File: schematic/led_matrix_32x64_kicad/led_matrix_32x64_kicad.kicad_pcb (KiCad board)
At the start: 2 copper layers, 6 parts, among them J1 LED Interface, J2 RTC, J3 INTERFACE, SW3 RESET, U1 Pico

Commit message: Snapshot before flipping the board
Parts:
- added C2: 1u, Capacitor_SMD:C_0805_2012Metric_Pad1.18x1.45mm_HandSolder, F.Cu at (114.7, 66.0)
- added C3: 1u, Capacitor_SMD:C_0805_2012Metric_Pad1.18x1.45mm_HandSolder, F.Cu at (116.0, 79.6)
- added J4: LEDPWR, Connector_PinHeader_2.54mm:PinHeader_1x02_P2.54mm_Horizontal, B.Cu at (115.3, 62.5)
- added R1: 10k, Resistor_SMD:R_0805_2012Metric_Pad1.20x1.40mm_HandSolder, F.Cu at (115.1, 75.6)
- added U2: NCP380, Package_SO:TSOP-5_1.65x3.05mm_P0.95mm, F.Cu at (114.7, 71.1)
- moved C1 47.5 mm to (116.6, 93.3), turned to 180 degrees
- moved SW3 28.4 mm to (110.9, 80.0), turned to 180 degrees
- moved J1 6.91 mm to (53.7, 71.1)
- moved J2 6.91 mm to (56.3, 100.3)
- moved J3 6.91 mm to (62.6, 87.6)
- moved U1 6.91 mm to (94.4, 78.7)
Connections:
- C1 pad 1: /5V -> /OUT
- U1 pad 29: unconnected-(U1-Pad29) -> /OVR
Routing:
- net GND: track 59.5 -> 283.7 mm, vias 0 -> 1
- net /3.3V: track 0.00 -> 81.3 mm, vias 0 -> 2
- net /SDA: track 0.00 -> 70.4 mm, vias 0 -> 2
- net /5V: track 0.00 -> 38.2 mm
- net /OUT: track 0.00 -> 36.0 mm
- net /OVR: track 0.00 -> 20.5 mm, vias 0 -> 2
- net /RUN: track 0.00 -> 7.62 mm
- net /G1: track 90.2 -> 86.7 mm
- net /EN: track 0.00 -> 3.42 mm
- net /G2: track 88.7 -> 85.5 mm
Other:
- board outline added: 68.6 x 60.3 mm

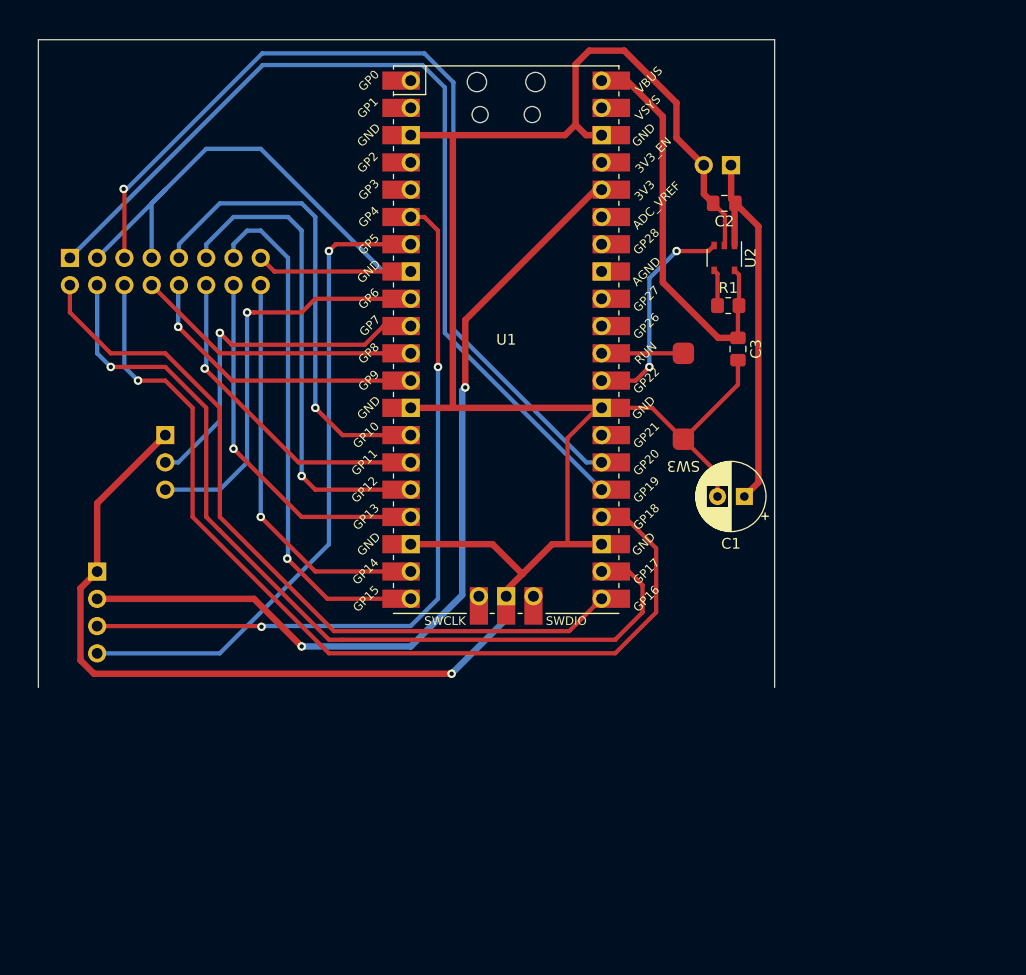
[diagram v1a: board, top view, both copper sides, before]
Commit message: New layout is getting closer
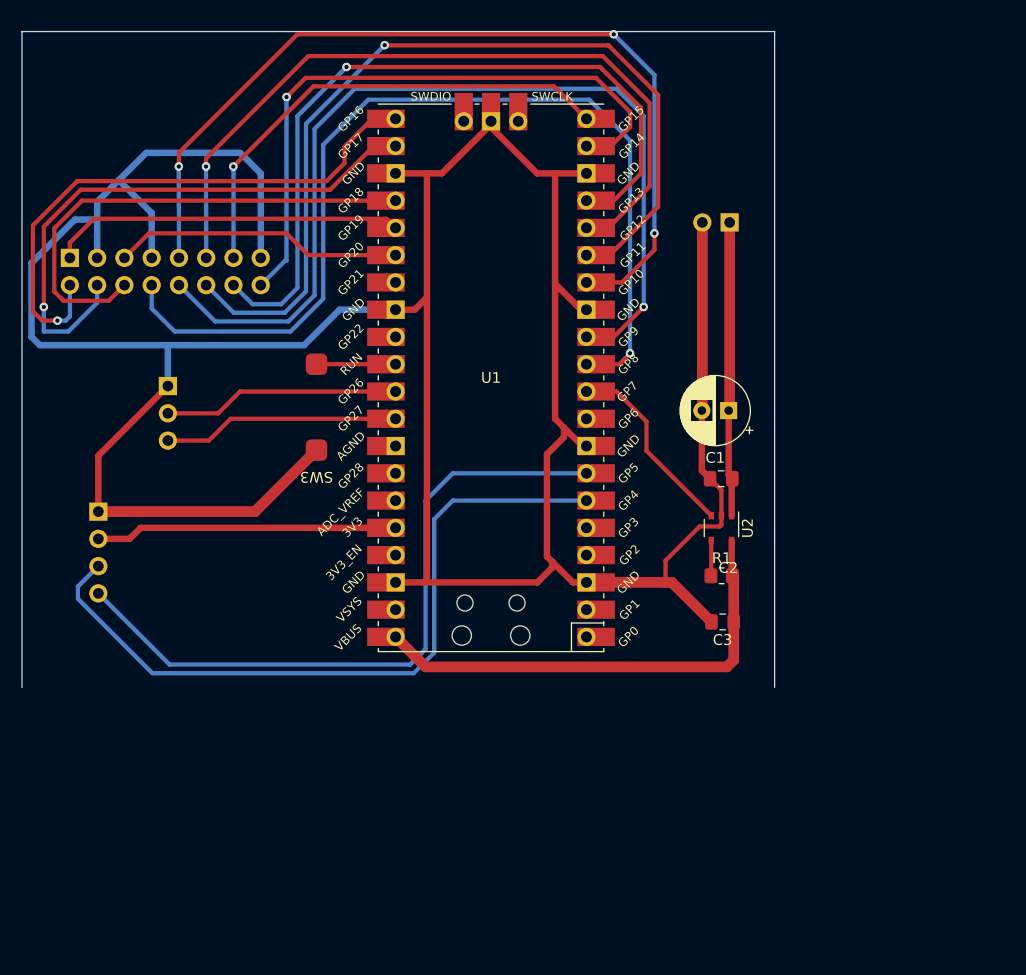
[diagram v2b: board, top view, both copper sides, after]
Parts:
- moved SW3 34.2 mm to (76.7, 81.0)
- moved C2 25.7 mm to (114.4, 91.7)
- moved C3 25.5 mm to (114.5, 105.0), turned to 180 degrees
- moved R1 25.2 mm to (114.4, 100.7)
- moved U2 25.2 mm to (114.4, 96.3)
- moved C1 8.13 mm to (115.1, 85.3)
- moved J2 5.59 mm to (56.4, 94.8)
- moved J4 5.34 mm to (115.2, 67.8)
- moved J3 4.58 mm to (62.9, 83.1)
- moved U1 3.83 mm to (93.0, 82.3), turned to 180 degrees
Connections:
- U1 pad 10: /INC -> /OVR
- U1 pad 29: /OVR -> unconnected-(U1-Pad29)
- U1 pad 31: unconnected-(U1-Pad31) -> /INC
- U1 pad 32: unconnected-(U1-Pad32) -> /SEL
- U1 pad 9: /SEL -> unconnected-(U1-Pad9)
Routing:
- net /B2: track 26.8 -> 90.9 mm, vias 0 -> 1
- net /HA: track 27.6 -> 88.1 mm
- net /G2: track 85.5 -> 27.0 mm, vias 1 -> 0
- net /G1: track 86.7 -> 33.0 mm
- net /3.3V: track 81.3 -> 28.1 mm, vias 2 -> 0
- net /HC: track 30.7 -> 83.5 mm
- net /R2: track 88.0 -> 46.2 mm, vias 1 -> 0
- net /HB: track 43.8 -> 84.1 mm, vias 1 -> 3
- net /CLK: track 34.4 -> 71.0 mm
- net /B1: track 82.1 -> 53.6 mm
- net /HD: track 45.3 -> 71.6 mm
- net GND: track 283.7 -> 309.2 mm, vias 1 -> 0
- net /OE: track 37.7 -> 58.8 mm
- net /R1: track 71.6 -> 53.7 mm, vias 0 -> 1
- net /SEL: track 38.4 -> 22.1 mm, vias 1 -> 0
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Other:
- board size 68.6 x 60.3 mm -> 70.1 x 61.1 mm

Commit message: More progress on PCB
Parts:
- C1: moved to B.Cu
- J4: moved to F.Cu
- moved J4 2.54 mm to (112.6, 67.8)
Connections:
- J4 pad 1: /OUT -> GND
- J4 pad 2: GND -> /OUT
- U2 pad 2: GND -> unconnected-(U2-Pad2)
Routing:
- net GND: track 309.2 -> 312.6 mm, vias 0 -> 16
- added copper zone on B.Cu, net GND
- added copper zone on F.Cu, net GND
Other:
- board size 70.1 x 61.1 mm -> 70.1 x 62 mm
- board text added: "3.3V"
- board text added: "5V"
- board text added: "B1"
- board text added: "B2"
- board text added: "CLK"
- board text added: "G1"
- board text added: "G2"
- board text added: "GND"
- board text added: "HA"
- board text added: "HB"
- board text added: "HC"
- board text added: "HD"
- board text added: "INC"
- board text added: "LAT"
- board text added: "LED Matrix Driver By: Matt Wachowski"
- board text added: "OE"
- board text added: "R1"
- board text added: "R2"
- board text added: "RUN"
- board text added: "SCL"
- board text added: "SDA"
- board text added: "SEL"

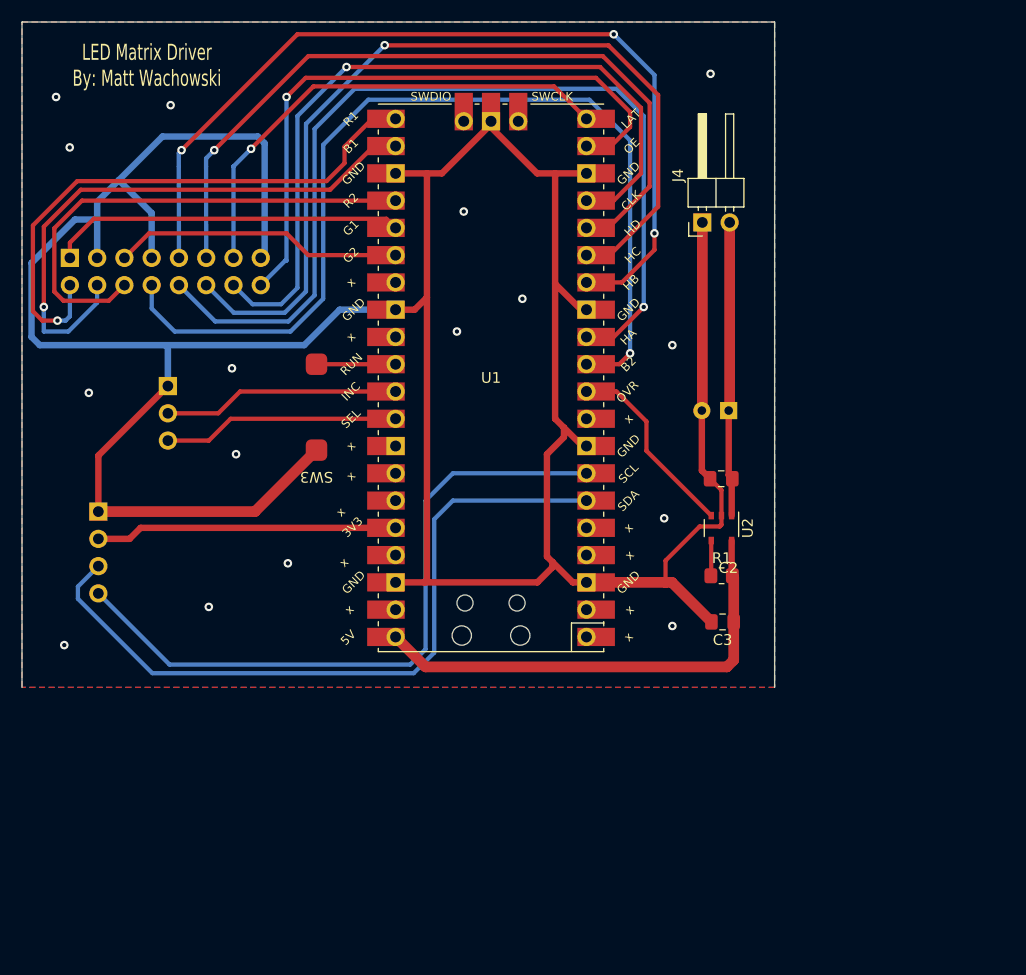
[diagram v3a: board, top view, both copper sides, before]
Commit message: Moved RTC clock pins.  Worked on labeling.
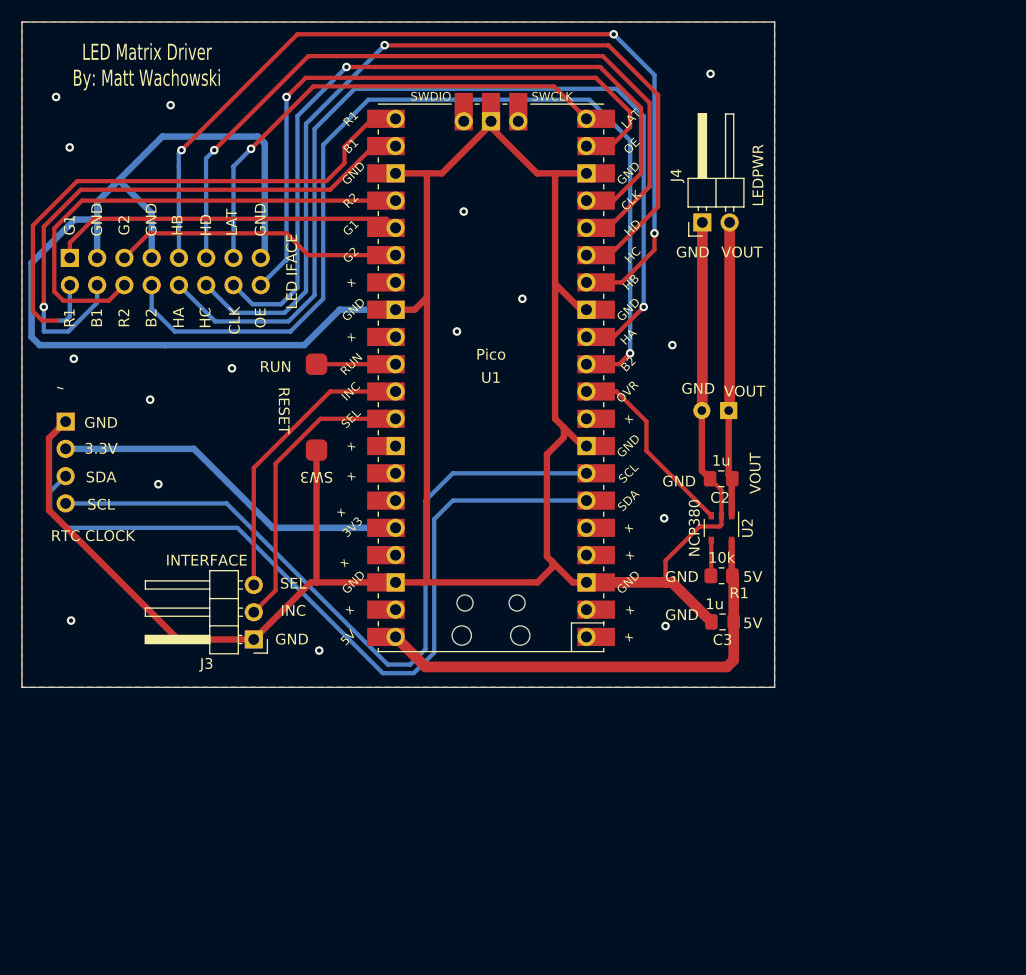
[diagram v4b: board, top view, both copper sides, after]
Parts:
- C1 220u: renamed from C1
- J3: moved to F.Cu
- moved J3 24.9 mm to (70.9, 106.7)
- moved J2 8.92 mm to (53.3, 86.4)
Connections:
- J3 pad 2: /INC -> /SEL
- J3 pad 3: /SEL -> /INC
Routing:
- net GND: track 312.6 -> 332.3 mm, vias 16 -> 15
- net /SCL: track 63.7 -> 70.2 mm
- net /SDA: track 68.0 -> 74.0 mm
- net /3.3V: track 28.1 -> 33.8 mm
- net /SEL: track 22.1 -> 27.6 mm
- net /INC: track 22.1 -> 27.1 mm
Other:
- outline, holes or cut-outs redrawn
- board text added: "OVR"
- board text added: "RTC CLOCK"
- board text added: "VOUT"

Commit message: Passing ERC and DRC checks
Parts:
- C1: renamed from C1 220u
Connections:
- U2 pad 2: unconnected-(U2-Pad2) -> GND
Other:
- outline, holes or cut-outs redrawn
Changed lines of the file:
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@@
   (net 37 "/EN")
   (net 38 "/OUT")
-  (net 39 "unconnected-(U2-Pad2)")
   (footprint "Capacitor_SMD:C_0805_2012Metric_Pad1.18x1.45mm_HandSolder" (layer "F.Cu")
     (at 114.5325 105.029 180)
@@
       (net 38 "/OUT") (pinfunction "OUT") (pintype "power_out"))
     (pad "2" smd rect (at -1.16 0 270) (size 0.7 0.51) (layers "F.Cu" "F.Paste" "F.Mask")
-      (net 39 "unconnected-(U2-Pad2)") (pinfunction "GND") (pintype "power_in"))
+      (net 3 "GND") (pinfunction "GND") (pintype "power_in"))
     (pad "3" smd rect (at -1.16 0.95 270) (size 0.7 0.51) (layers "F.Cu" "F.Paste" "F.Mask")
       (net 36 "/OVR") (pinfunction "~{FLAG}") (pintype "output"))
@@
     (property "Sheetname" "")
     (attr through_hole)
-    (fp_text reference "C1 220u" (at 1.25 4.4) (layer "B.SilkS")
+    (fp_text reference "C1" (at 1.25 4.4) (layer "B.SilkS")
       (effects (font (size 1 1) (thickness 0.15)) (justify mirror))
     )
@@
   (gr_line (start 49.276 111.125) (end 119.38 111.125) (layer "Edge.Cuts") (width 0.1))
   (gr_line (start 49.276 49.149) (end 49.276 111.125) (layer "Edge.Cuts") (width 0.1))
-  (gr_line (start 52.578 83.185) (end 53.086 83.312) (layer "Edge.Cuts") (width 0.1))
   (gr_text "INC" (at 80.264 83.566) (layer "B.SilkS")
     (effects (font (size 1 1) (thickness 0.15)) (justify mirror))
@@
   (segment (start 79.317315 62.299315) (end 77.64663 63.97) (width 0.4) (layer "F.Cu") (net 17))
   (segment (start 81.914 58.166) (end 79.317315 60.762685) (width 0.4) (layer "F.Cu") (net 17))
-  (via (at 54.102 80.518) (size 0.8) (drill 0.4) (layers "F.Cu" "B.Cu") (net 17))
+  (via (at 52.578 76.962) (size 0.8) (drill 0.4) (layers "F.Cu" "B.Cu") (net 17))
   (segment (start 53.735 76.567) (end 53.34 76.962) (width 0.4) (layer "B.Cu") (net 17))
   (segment (start 53.34 76.962) (end 52.578 76.962) (width 0.4) (layer "B.Cu") (net 17))
   (segment (start 53.735 73.66) (end 53.735 76.567) (width 0.4) (layer "B.Cu") (net 17))
-  (segment (start 51.308 75.946) (end 51.308 75.692) (width 0.4) (layer "F.Cu") (net 18))
   (segment (start 82.042 60.706) (end 77.978 64.77) (width 0.4) (layer "F.Cu") (net 18))
   (segment (start 54.748629 64.77) (end 51.308 68.21063) (width 0.4) (layer "F.Cu") (net 18))
